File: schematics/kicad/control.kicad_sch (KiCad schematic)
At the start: 19 parts, among them U1000 PAL16R8, U1001 PAL20X10, U1002 PAL20X10, U1003 PAL20X10, U1004 PAL20R6, U1005 P16L8, U1006 PAL16R8, U1007 P20L8, U1008 P16L8, U1009 P16L8, U1010 P16L8, U1015 74F175, U1016 74F244, U1017 330Ω, U1021 330Ω, U1036 330Ω, U1037 330Ω, U1038 330Ω

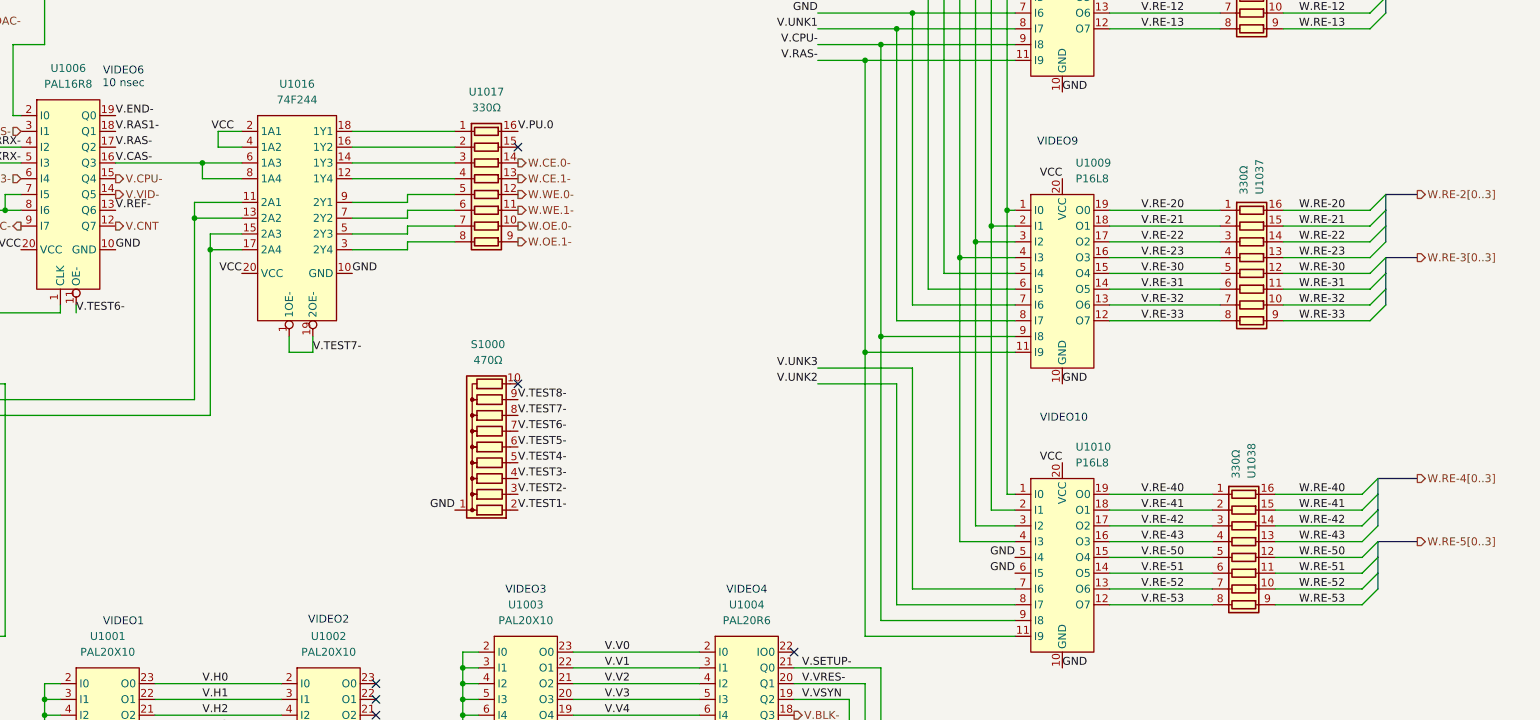
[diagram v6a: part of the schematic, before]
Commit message: Fix ERCs which uncovered some issues with W.RE for the overlay memory. Finish the ECL chips for clock control - need to find value of R1315. Add space for 0-ohm resistor on V.VSYN which exists in schematics but was never connected in the original composite sync scheme with 4 BNC connectors. Can leave it unconnected if it causes issues.
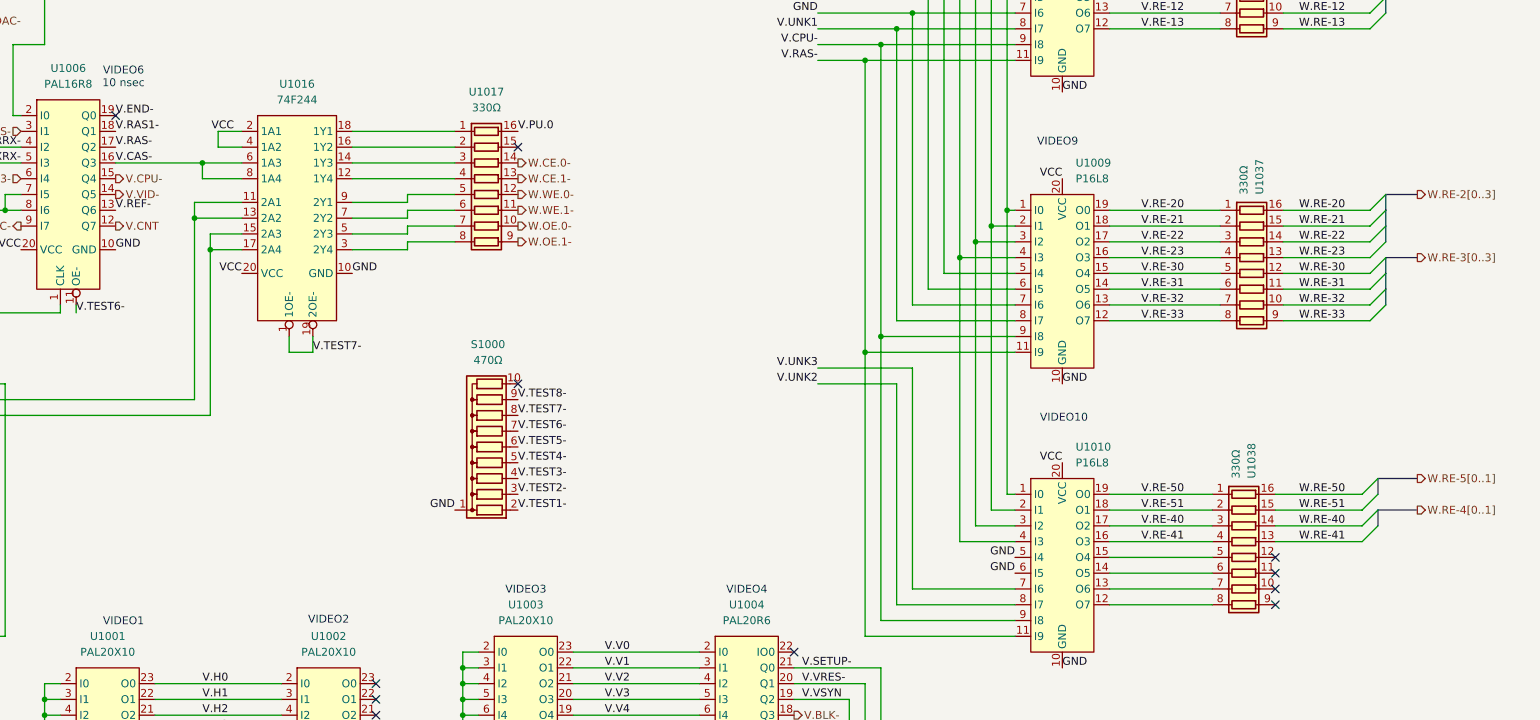
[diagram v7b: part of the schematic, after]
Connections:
- net V.RE-42 is gone; now on net V.RE-40: U1010.17 (O2), U1038.3 (R3.1)
- net V.RE-43 is gone; now on net V.RE-41: U1010.16 (O3), U1038.4 (R4.1)
- net W.RE-42 is gone; now on net W.RE-40: U1038.14 (R3.2)
- net W.RE-43 is gone; now on net W.RE-41: U1038.13 (R4.2)
- net V.RE-40: no longer U1010.19 (O0), U1038.1 (R1.1)
- net V.RE-41: no longer U1010.18 (O1), U1038.2 (R2.1)
- net V.RE-50: now also U1010.19 (O0), U1038.1 (R1.1); no longer U1010.15 (O4), U1038.5 (R5.1)
- net V.RE-51: now also U1010.18 (O1), U1038.2 (R2.1); no longer U1010.14 (O5), U1038.6 (R6.1)
- net W.RE-40: no longer U1038.16 (R1.2)
- net W.RE-41: no longer U1038.15 (R2.2)
- net W.RE-50: now also U1038.16 (R1.2); no longer U1038.12 (R5.2)
- net W.RE-51: now also U1038.15 (R2.2); no longer U1038.11 (R6.2)
- net V.RE-52: no longer names the net of U1010.13 (O6), U1038.7 (R7.1)
- net V.RE-53: no longer names the net of U1010.12 (O7), U1038.8 (R8.1)
- net W.RE-52: no longer names the net of U1038.10 (R7.2)
- net W.RE-53: no longer names the net of U1038.9 (R8.2)
- new net: U1010.15 (O4), U1038.5 (R5.1)
- new net: U1010.14 (O5), U1038.6 (R6.1)
- no-connect marks 20 -> 25

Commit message: Finish routing and misc fixes in the analog section
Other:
- moved on the sheet: S1000, U1000, U1001, U1002, U1003, U1004, U1005, U1006, U1007, U1015, U1016, U1017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
